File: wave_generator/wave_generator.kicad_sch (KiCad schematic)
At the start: 100 parts, among them J1 KF301_3PIN_POWER, J2 KF301_2PIN_INPUT, J3 KF301_2PIN_INPUT, J4 KF301_2PIN_OUTPUT, J5 UART, J6 SWD, J7 TEST, U1 L7809, U2 LM7909, U3 AMS1117-3.3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

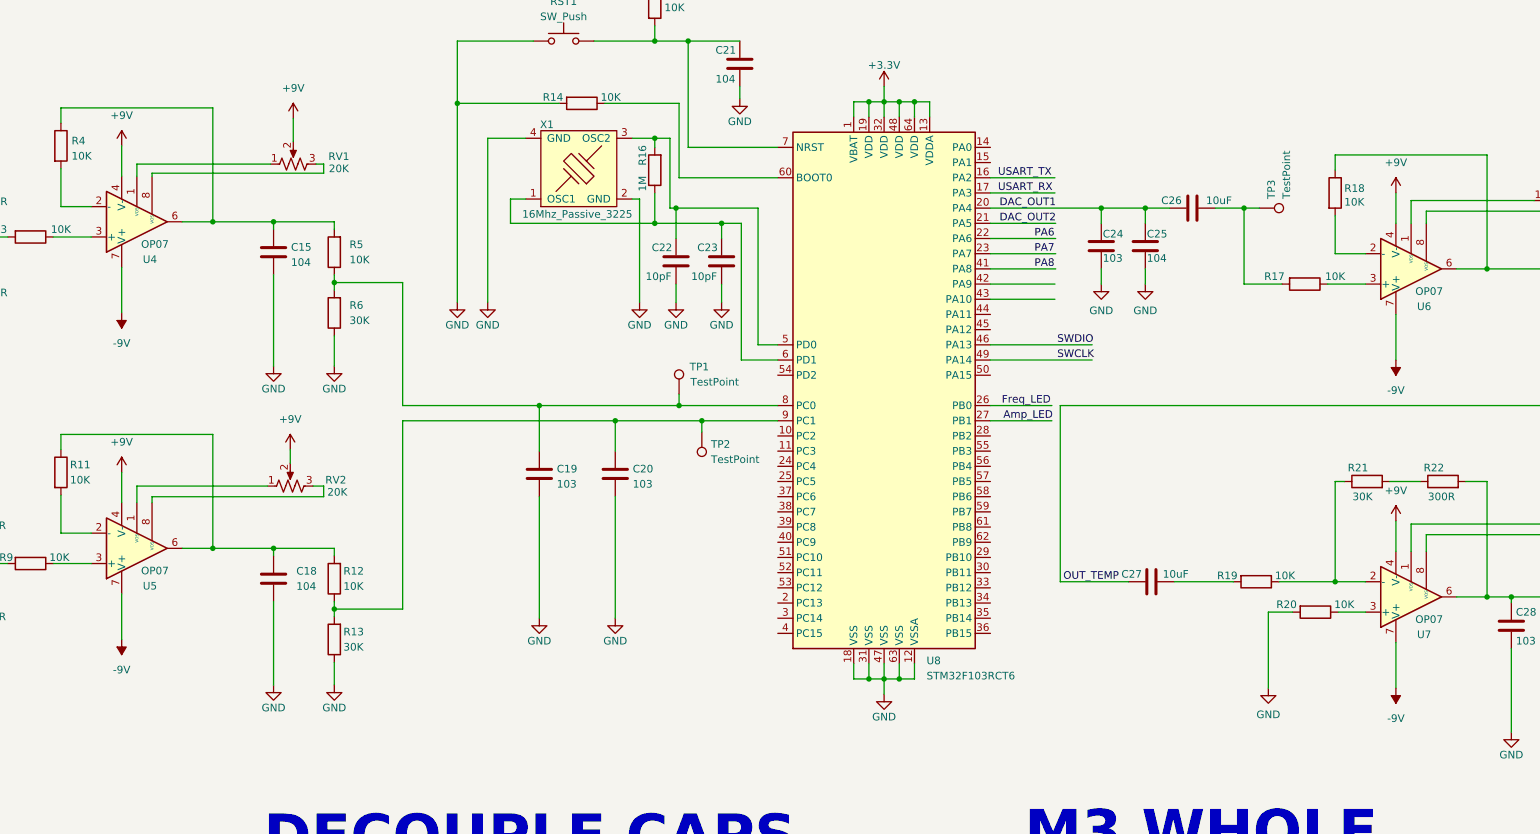
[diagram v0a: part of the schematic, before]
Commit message: fixed hardware error
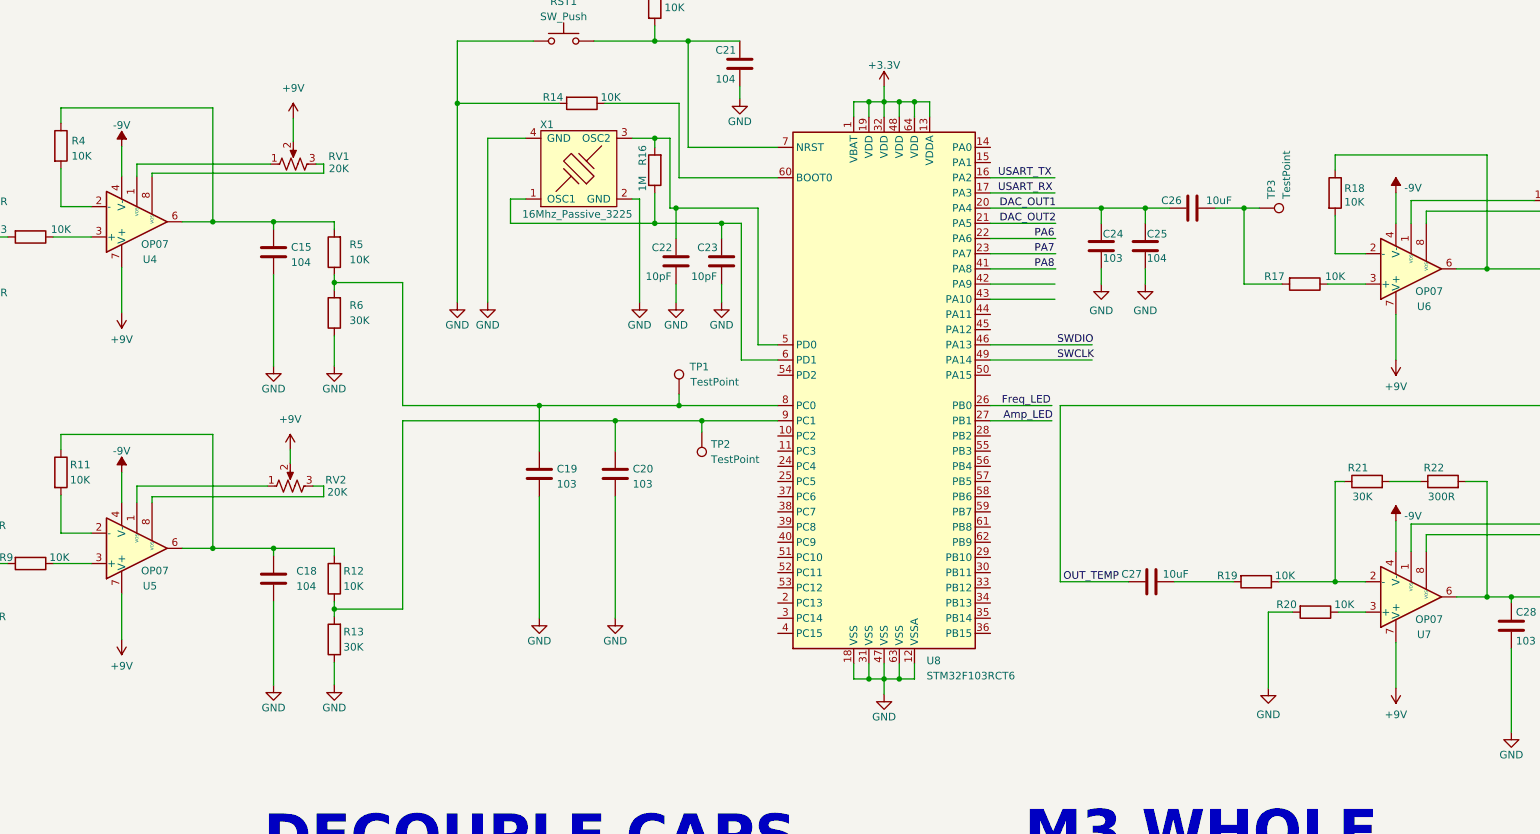
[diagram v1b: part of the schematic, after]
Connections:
- net +9V: now also U4.7 (V+), U5.7 (V+), U6.7 (V+), U7.7 (V+); no longer U4.4 (V-), U5.4 (V-), U6.4 (V-), U7.4 (V-)
- net -9V: now also U4.4 (V-), U5.4 (V-), U6.4 (V-), U7.4 (V-); no longer U4.7 (V+), U5.7 (V+), U6.7 (V+), U7.7 (V+)
